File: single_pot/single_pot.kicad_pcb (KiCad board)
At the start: 2 copper layers, 24.2 x 18 mm, 5 parts, among them J1 I/O connector

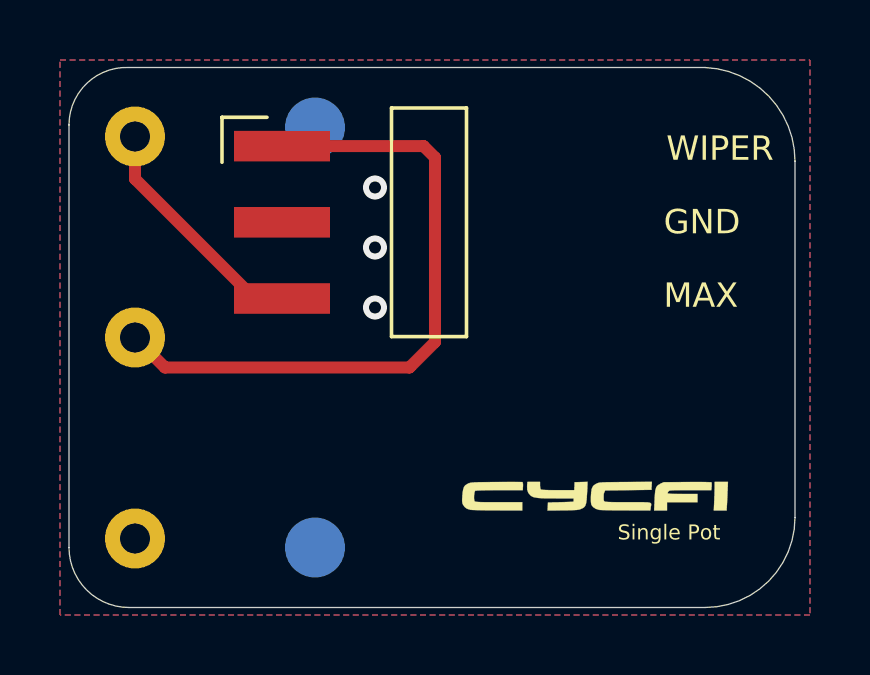
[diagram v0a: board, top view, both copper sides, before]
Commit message: Added taper resistor
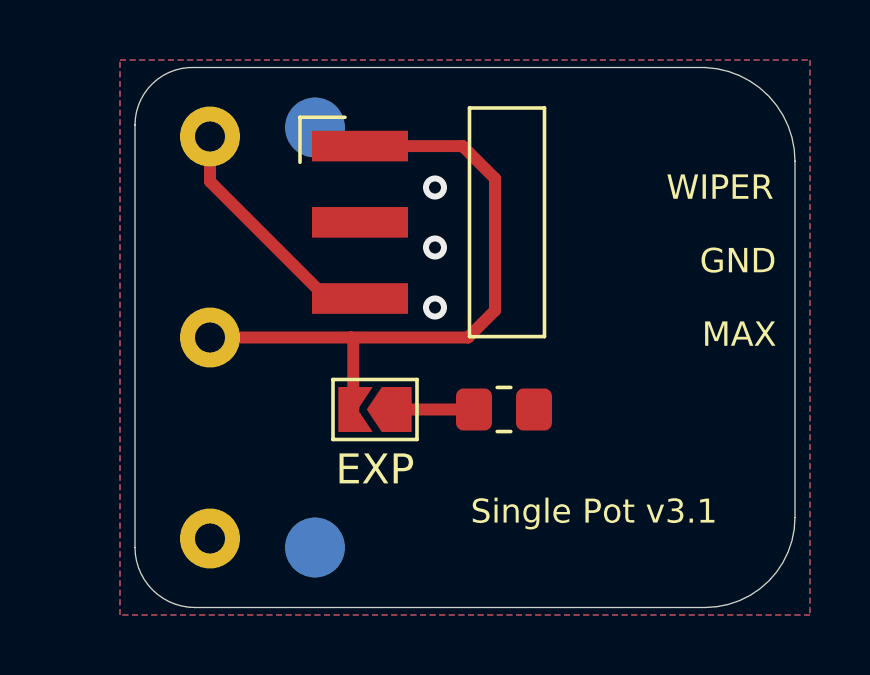
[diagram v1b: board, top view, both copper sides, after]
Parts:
- removed G***: LOGO, cycfi_library:cycfi-logo-9mm
- added JP1: SolderJumper_2_Open, Jumper:SolderJumper-2_P1.3mm_Open_TrianglePad1.0x1.5mm, F.Cu at (144.0, 82.4)
- added R1: 4.7k, Resistor_SMD:R_0805_2012Metric_Pad1.20x1.40mm_HandSolder, F.Cu at (148.3, 82.4)
- RV1: value 25k -> 500k
- moved J1 2.60 mm to (143.5, 73.6)
- moved RV1 2.50 mm to (138.5, 80.0)
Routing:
- net Net-(JP1-Pad1): track 0.00 -> 2.58 mm
- net WIPER: track 22.2 -> 21.7 mm
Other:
- board size 24.2 x 18 mm -> 22 x 18 mm
- board text added: "EXP"
- board text added: "Single Pot v3.1"
- board text removed: "Single Pot"

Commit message: Update to v3.1
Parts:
- added G***: LOGO, cycfi_library:cycfi-logo-9mm, F.Cu at (150.7, 85.7)
- R1: value 4.7k -> 100k
